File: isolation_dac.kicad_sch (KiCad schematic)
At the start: 28 parts, among them IC1 DAC63204RTERQ1, IC2 ISO7641FMDWR, IC5 REF35409QDBVR, J4 Conn_01x03, T1 760390015, U3 TPS76350DBVRG4

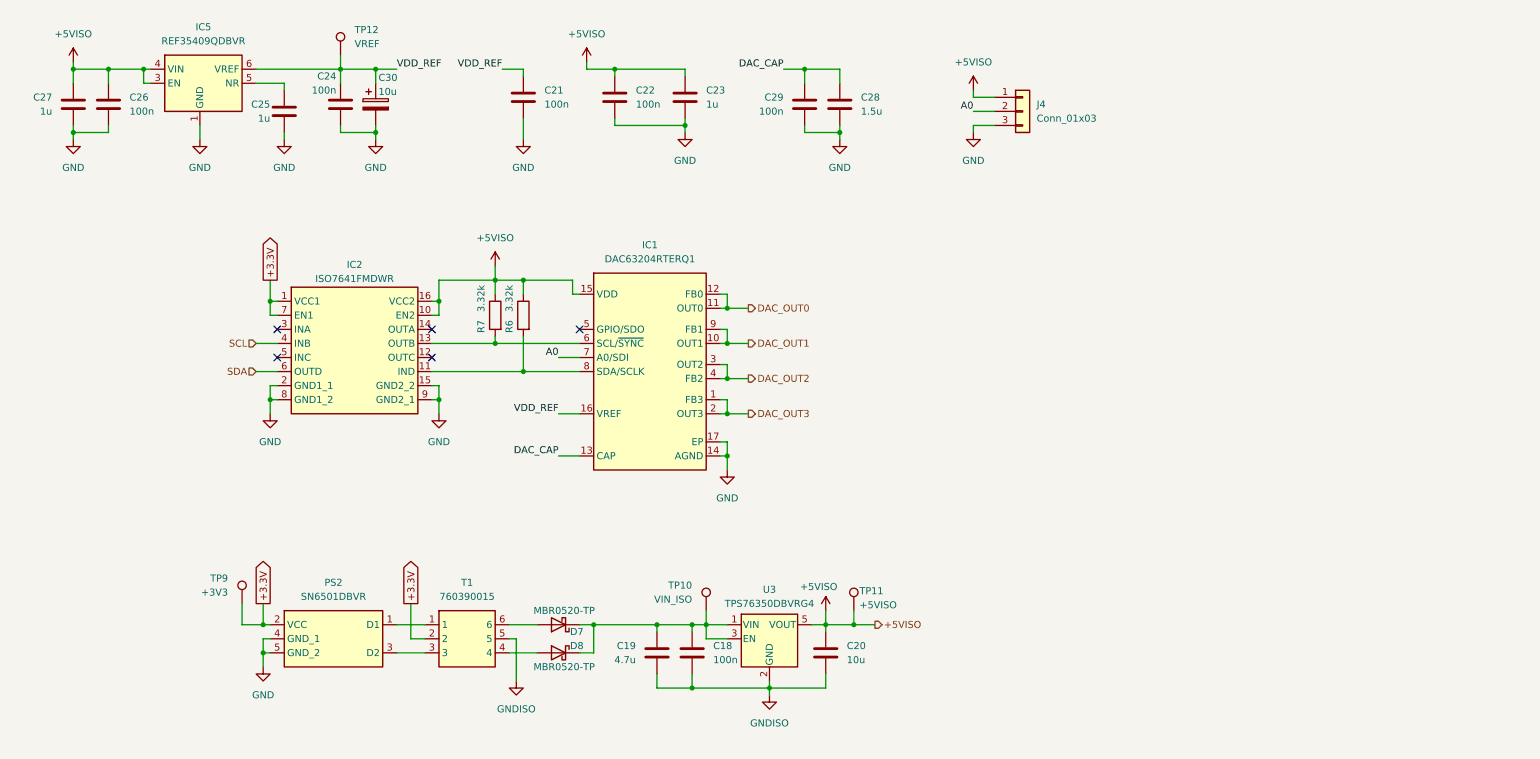
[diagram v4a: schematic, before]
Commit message: fix: replacement of ISO7641 with ISO7640
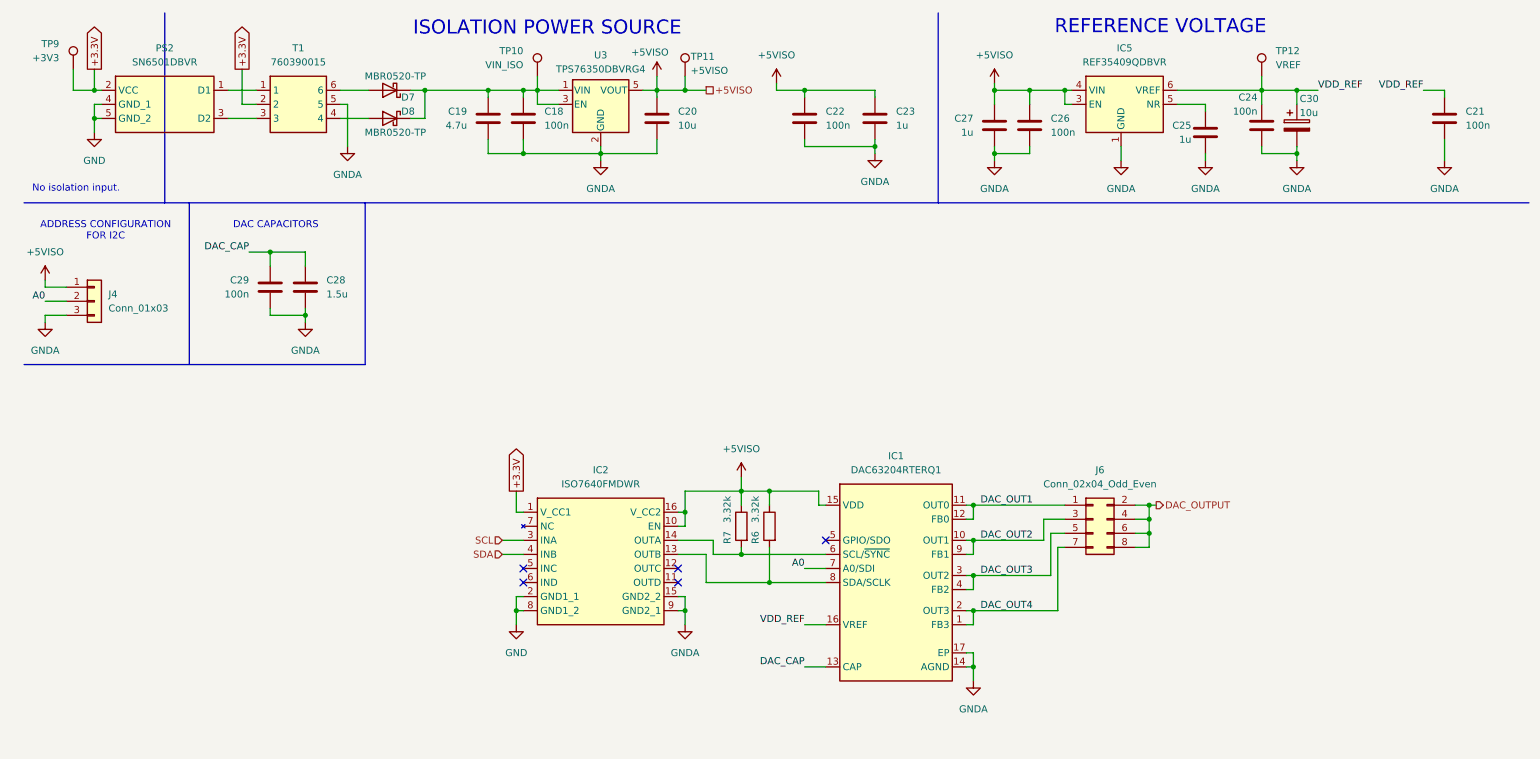
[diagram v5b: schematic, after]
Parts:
- removed IC2: ISO7641FMDWR, Package_SO:SOIC-16W_7.5x10.3mm_P1.27mm, symbol techstim:ISO7641FMDWR
- added IC2: ISO7640FMDWR, Package_SO:SOIC-16W_7.5x10.3mm_P1.27mm, symbol Technaid:ISO7640FMDWR
- added J6: Conn_02x04_Odd_Even, Connector_PinHeader_2.54mm:PinHeader_2x04_P2.54mm_Vertical, symbol Connector_Generic:Conn_02x04_Odd_Even
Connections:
- net DAC_OUT0 is gone; now on net DAC_OUT1: IC1.11 (OUT0), IC1.12 (FB0)
- net GNDISO is gone; now on net GND: C18.1, C19.2, C20.1, T1.5, U3.2 (GND)
- net +3.3V: now also IC2.1 (V_CC1)
- net +5VISO: now also IC2.10 (EN), IC2.16 (V_CC2)
- net DAC_OUT1: now also J6.1 (Pin_1); no longer IC1.10 (OUT1), IC1.9 (FB1)
- net DAC_OUT2: now also IC1.10 (OUT1), IC1.9 (FB1), J6.3 (Pin_3); no longer IC1.3 (OUT2), IC1.4 (FB2)
- net DAC_OUT3: now also IC1.3 (OUT2), IC1.4 (FB2), J6.5 (Pin_5); no longer IC1.1 (FB3), IC1.2 (OUT3)
- net GND: now also IC2.15 (GND2_2), IC2.2 (GND1_1), IC2.8 (GND1_2), IC2.9 (GND2_1)
- net SCL: now also IC2.3 (INA)
- net SDA: now also IC2.4 (INB)
- net at IC1.8 (SDA/SCLK), R6.2: now also IC2.13 (OUTB)
- net at IC1.6 (SCL/~{SYNC}), R7.2: now also IC2.14 (OUTA)
- new net DAC_OUT4: IC1.1 (FB3), IC1.2 (OUT3), J6.7 (Pin_7)
- new net DAC_OUTPUT: J6.2 (Pin_2), J6.4 (Pin_4), J6.6 (Pin_6), J6.8 (Pin_8)
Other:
- note added: "ADDRESS CONFIGURATION FOR I2C"
- note added: "DAC CAPACITORS"
- note added: "ISOLATION POWER SOURCE"
- note added: "No isolation input."
- note added: "REFERENCE VOLTAGE"
- moved on the sheet: C18, C19, C20, C21, C22, C23, C24, C25, C26, C27, C28, C29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

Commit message: fix: update PCB with last 3dmodels and ICs (ISO7640, GNDISO)
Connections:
- net GND: no longer C18.1, C19.2, C20.1, C21.1, C22.1, C23.1, C24.1, C25.1, C26.1, C27.1, C28.1, C29.1, C30.2, IC1.14 (AGND), IC1.17 (EP), IC2.15 (GND2_2), IC2.9 (GND2_1), IC5.1 (GND), IC5.2 (GND), J4.3 (Pin_3), T1.5, U3.2 (GND)
- new net GNDISO: C18.1, C19.2, C20.1, C21.1, C22.1, C23.1, C24.1, C25.1, C26.1, C27.1, C28.1, C29.1, C30.2, IC1.14 (AGND), IC1.17 (EP), IC2.15 (GND2_2), IC2.9 (GND2_1), IC5.1 (GND), IC5.2 (GND), J4.3 (Pin_3), T1.5, U3.2 (GND)

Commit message: docs: update S1L, S1N, MFP, MFN
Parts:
- J6: MFN (none) -> Samtec; MFP (none) -> TSW-102-07-T-D; S1PL (none) -> https://eu.mouser.com/ProductDetail/Samtec/TSW-102-07-T-D?q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; S1PN (none) -> Mouser
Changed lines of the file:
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@@
 	(wire
 		(pts
-			(xy 102.87 102.87) (xy 101.6 102.87)
+			(xy 101.6 102.87) (xy 102.87 102.87)
 		)
 		(stroke
@@
 	(wire
 		(pts
+			(xy 101.6 99.06) (xy 101.6 102.87)
+		)
+		(stroke
+			(width 0)
+			(type default)
+		)
+	)
+	(wire
+		(pts
 			(xy 153.67 26.67) (xy 153.67 27.94)
 		)
@@
 	(wire
 		(pts
+			(xy 99.06 107.95) (xy 102.87 107.95)
+		)
+		(stroke
+			(width 0)
+			(type default)
+		)
+	)
+	(wire
+		(pts
 			(xy 269.24 27.94) (xy 269.24 26.67)
 		)
@@
 		)
 	)
-	(wire
-		(pts
-			(xy 99.06 107.95) (xy 102.87 107.95)
-		)
-		(stroke
-			(width 0)
-			(type default)
-		)
-	)
 	(polyline
 		(pts
@@
 	(wire
 		(pts
+			(xy 26.67 26.67) (xy 25.4 26.67)
+		)
+		(stroke
+			(width 0)
+			(type default)
+		)
+	)
+	(wire
+		(pts
+			(xy 102.87 118.11) (xy 101.6 118.11)
+		)
+		(stroke
+			(width 0)
+			(type default)
+		)
+	)
+	(wire
+		(pts
+			(xy 102.87 35.56) (xy 102.87 38.1)
+		)
+		(stroke
+			(width 0)
+			(type default)
+		)
+	)
+	(wire
+		(pts
+			(xy 166.37 26.67) (xy 153.67 26.67)
+		)
+		(stroke
+			(width 0)
+			(type default)
+		)
+	)
+	(polyline
+		(pts
+			(xy 38.1 12.7) (xy 38.1 46.99)
+		)
+		(stroke
+			(width 0)
+			(type default)
+		)
+	)
+	(wire
+		(pts
+			(xy 215.9 101.6) (xy 217.17 101.6)
+		)
+		(stroke
+			(width 0)
+			(type default)
+		)
+	)
+	(wire
+		(pts
+			(xy 142.24 99.06) (xy 142.24 101.6)
+		)
+		(stroke
+			(width 0)
+			(type default)
+		)
+	)
+	(wire
+		(pts
+			(xy 142.24 99.06) (xy 142.24 96.52)
+		)
+		(stroke
+			(width 0)
+			(type default)
+		)
+	)
+	(wire
+		(pts
+			(xy 142.24 109.22) (xy 142.24 110.49)
+		)
+		(stroke
+			(width 0)
+			(type default)
+		)
+	)
+	(wire
+		(pts
+			(xy 184.15 114.3) (xy 184.15 116.84)
+		)
+		(stroke
+			(width 0)
+			(type default)
+		)
+	)
+	(wire
+		(pts
 			(xy 99.06 110.49) (xy 102.87 110.49)
 		)
@@
 	(wire
 		(pts
-			(xy 26.67 26.67) (xy 25.4 26.67)
-		)
-		(stroke
-			(width 0)
-			(type default)
-		)
-	)
-	(wire
-		(pts
-			(xy 102.87 118.11) (xy 101.6 118.11)
-		)
-		(stroke
-			(width 0)
-			(type default)
-		)
-	)
-	(wire
-		(pts
-			(xy 102.87 35.56) (xy 102.87 38.1)
-		)
-		(stroke
-			(width 0)
-			(type default)
-		)
-	)
-	(wire
-		(pts
-			(xy 166.37 26.67) (xy 153.67 26.67)
-		)
-		(stroke
-			(width 0)
-			(type default)
-		)
-	)
-	(polyline
-		(pts
-			(xy 38.1 12.7) (xy 38.1 46.99)
-		)
-		(stroke
-			(width 0)
-			(type default)
-		)
-	)
-	(wire
-		(pts
-			(xy 215.9 101.6) (xy 217.17 101.6)
-		)
-		(stroke
-			(width 0)
-			(type default)
-		)
-	)
-	(wire
-		(pts
-			(xy 142.24 99.06) (xy 142.24 101.6)
-		)
-		(stroke
-			(width 0)
-			(type default)
-		)
-	)
-	(wire
-		(pts
-			(xy 142.24 99.06) (xy 142.24 96.52)
-		)
-		(stroke
-			(width 0)
-			(type default)
-		)
-	)
-	(wire
-		(pts
-			(xy 142.24 109.22) (xy 142.24 110.49)
-		)
-		(stroke
-			(width 0)
-			(type default)
-		)
-	)
-	(wire
-		(pts
-			(xy 184.15 114.3) (xy 184.15 116.84)
-		)
-		(stroke
-			(width 0)
-			(type default)
-		)
-	)
-	(wire
-		(pts
 			(xy 196.85 104.14) (xy 200.66 104.14)
 		)
@@
 		(pts
 			(xy 130.81 110.49) (xy 135.89 110.49)
-		)
-		(stroke
-			(width 0)
-			(type default)
-		)
-	)
-	(wire
-		(pts
-			(xy 101.6 102.87) (xy 101.6 99.06)
 		)
 		(stroke
@@
 			)
 		)
-		(property "Datasheet" "~"
+		(property "Datasheet" "https://eu.mouser.com/datasheet/2/527/tsw_th-2854687.pdf"
 			(at 205.74 104.14 0)
 			(effects
@@
 			(at 205.74 104.14 0)
 			(effects
+				(font
+					(size 1.27 1.27)
+				)
+				(hide yes)
+			)
+		)
+		(property "MFN" "Samtec"
+			(at 205.74 104.14 0)
+			(effects
+				(font
+					(size 1.27 1.27)
+				)
+				(hide yes)
+			)
+		)
+		(property "MFP" "TSW-102-07-T-D"
+			(at 205.74 104.14 0)
+			(effects
+				(font
+					(size 1.27 1.27)
+				)
+				(hide yes)
+			)
+		)
+		(property "S1PN" "Mouser"
+			(at 205.74 104.14 0)
+			(effects
+				(font
+					(size 1.27 1.27)
+				)
+				(hide yes)
+			)
+		)
+		(property "S1PL" "https://eu.mouser.com/ProductDetail/Samtec/TSW-102-07-T-D?qs=FESYatJ8odLVnZ57cajWUg%3D%3D"
+			(at 205.74 104.14 0)
+			(effects

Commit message: docs: adding Note for choose  R_pull_up over I2C pins
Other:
- note added: "*"
- note added: "* R_p [1.5 - 8.11] kOhm. V_IL = 0.4 V (max) V_IH = 1.62 V (min) t_rise = 1000 ns C_p = 400 pF (standard)"
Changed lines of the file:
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@@
+		)
+	)
+	(text "*"
+		(exclude_from_sim no)
+		(at 146.304 109.728 0)
+		(effects
+			(font
+				(size 1.27 1.27)
+			)
+		)
+	)
+	(text "*"
+		(exclude_from_sim no)
+		(at 140.97 109.728 0)
+		(effects
+			(font
+				(size 1.27 1.27)
+			)
 		)
 	)
@@
 		)
 	)
+	(text "* R_p [1.5 - 8.11] kOhm.\nV_IL = 0.4 V (max)\nV_IH = 1.62 V (min)\nt_rise = 1000 ns\nC_p = 400 pF (standard)"
+		(exclude_from_sim no)
+		(at 153.162 140.208 0)
+		(effects
+			(font
+				(size 1.27 1.27)
+			)
+			(justify left)
+		)
+	)
